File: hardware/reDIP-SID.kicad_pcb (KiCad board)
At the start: 6 copper layers, 17.8 x 35.6 mm, 92 parts, among them J1 Conn_01x04, J2 Conn_01x04, J3 Conn_01x10, J4 Conn_01x10, J5 TYPE-C-31-M-12, J6 Conn_02x05_Odd_Even, Q1 PDTA143ZMB, SW1 KXT331LHS, U1 NCP163AMX120TBG, U2 NCP167AMX330TBG, U3 SN74CBTD16211DGVR, U4 SGTL5000XNLA3, U5 NUF2042XV6, U6 APS6404L-3SQR-SN, U7 W25Q128JVPIM, U8 ICE40UP5K-SG48I, X1 ASCO-24.576MHZ-EK-T

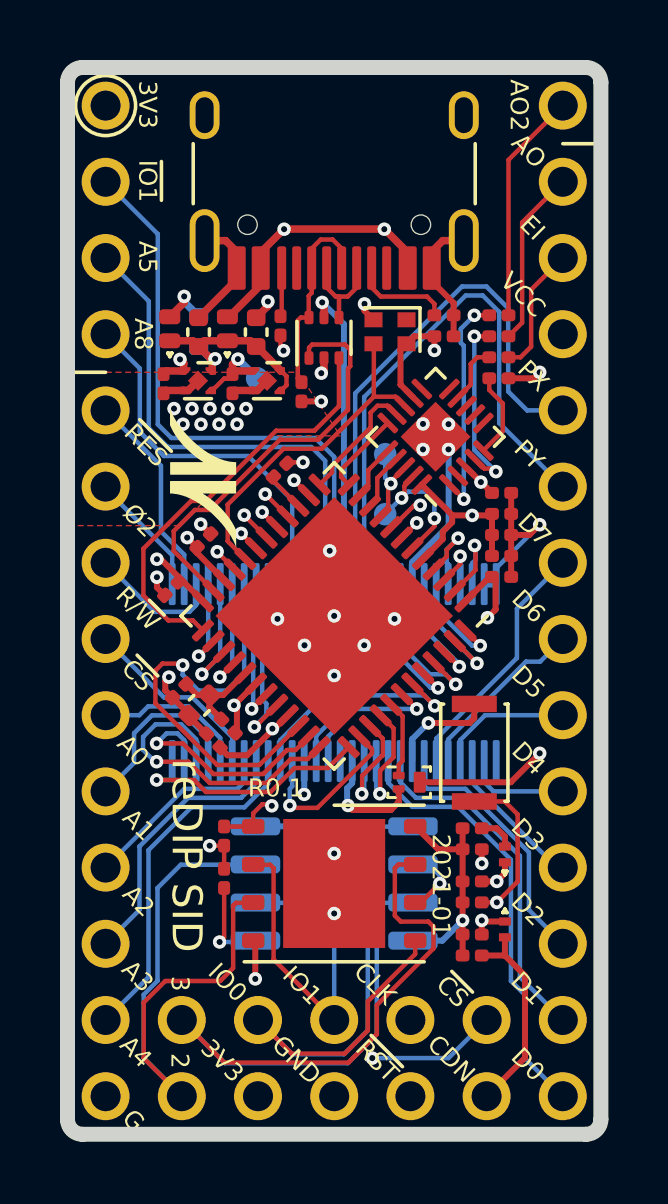
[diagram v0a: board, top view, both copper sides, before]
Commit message: Moved Vcc via away from pin-in-paste stencil aperture
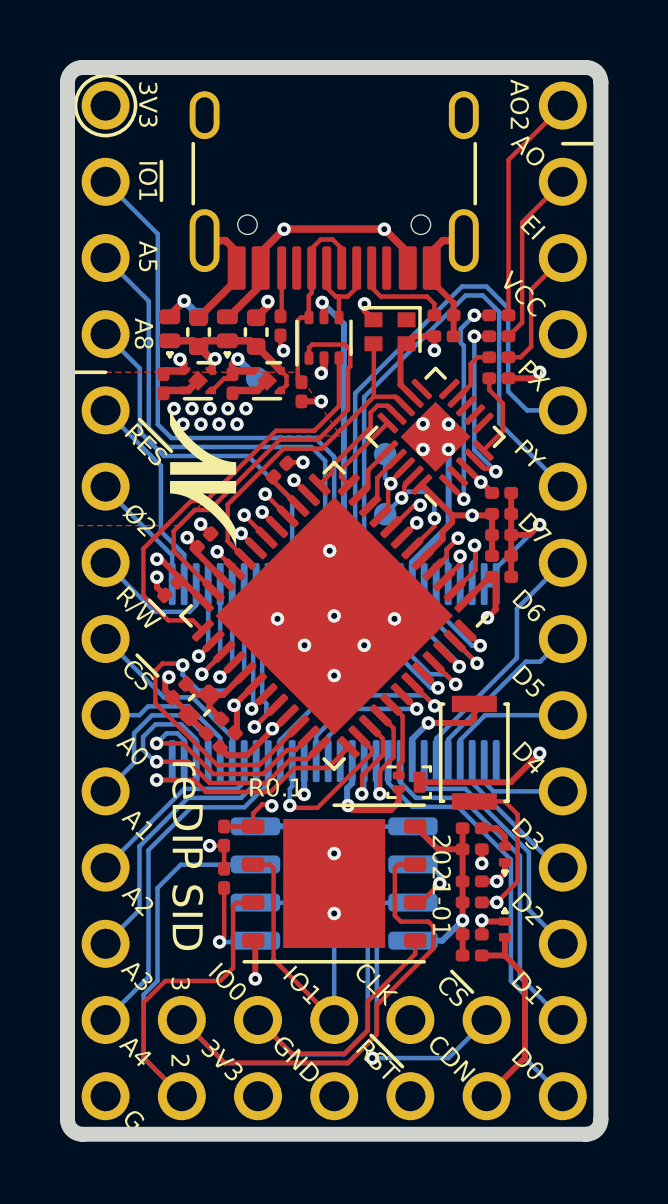
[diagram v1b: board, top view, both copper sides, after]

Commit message: Usability and manufacturability improvements
* Made all iCE40 RGB pins externally available
* Removed split in stencil apertures for pin-in-paste
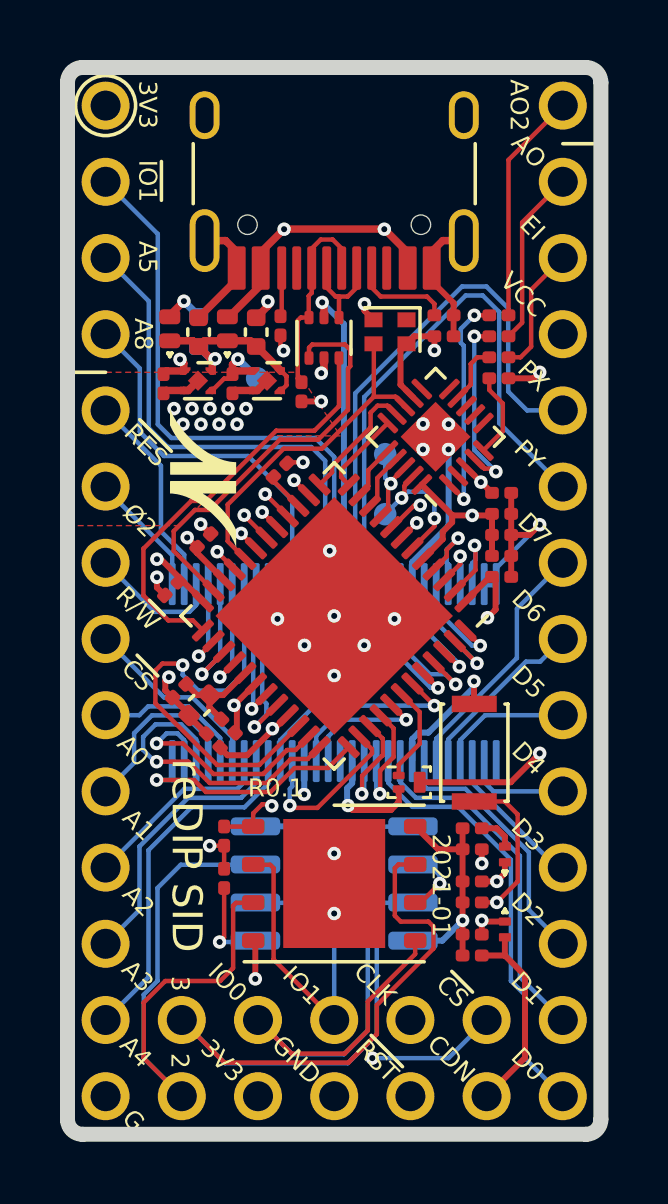
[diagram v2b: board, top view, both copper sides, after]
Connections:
- Q1 pad 1: /USB_CONN -> /USB_~CONN~
- U8 pad 41: /USB_CONN -> /ICE_~IO1~
- U8 pad 42: /ICE_~IO1~ -> /USB_~CONN~
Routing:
- net /USB_~CONN~: track 0.00 -> 3.31 mm
- net /USB_CONN: track 2.57 -> 0.00 mm
- net GND: track 48.4 -> 49.3 mm

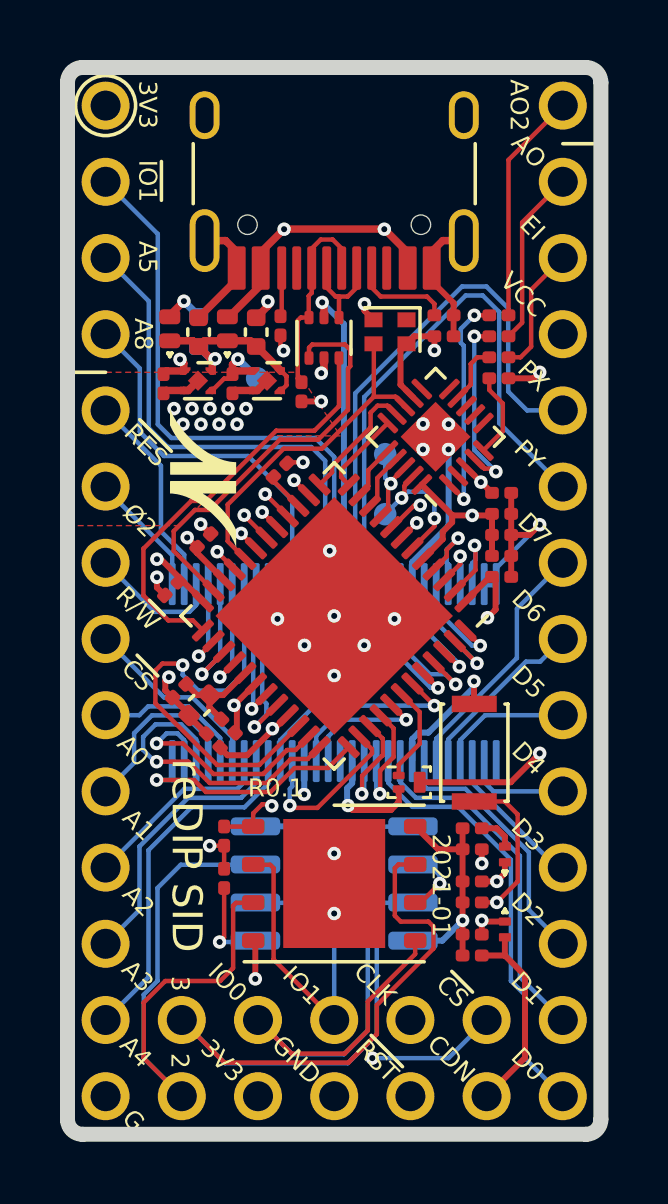
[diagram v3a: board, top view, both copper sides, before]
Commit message: Usability and manufacturability improvements
* Added extra vias for Vcc and 3.3V rails, for high power external devices
* Added extra thermal via for SGTL5000
* Assume 3x solder paste volume for paste-in-hole
* Adjustments to fab and silk screen layers
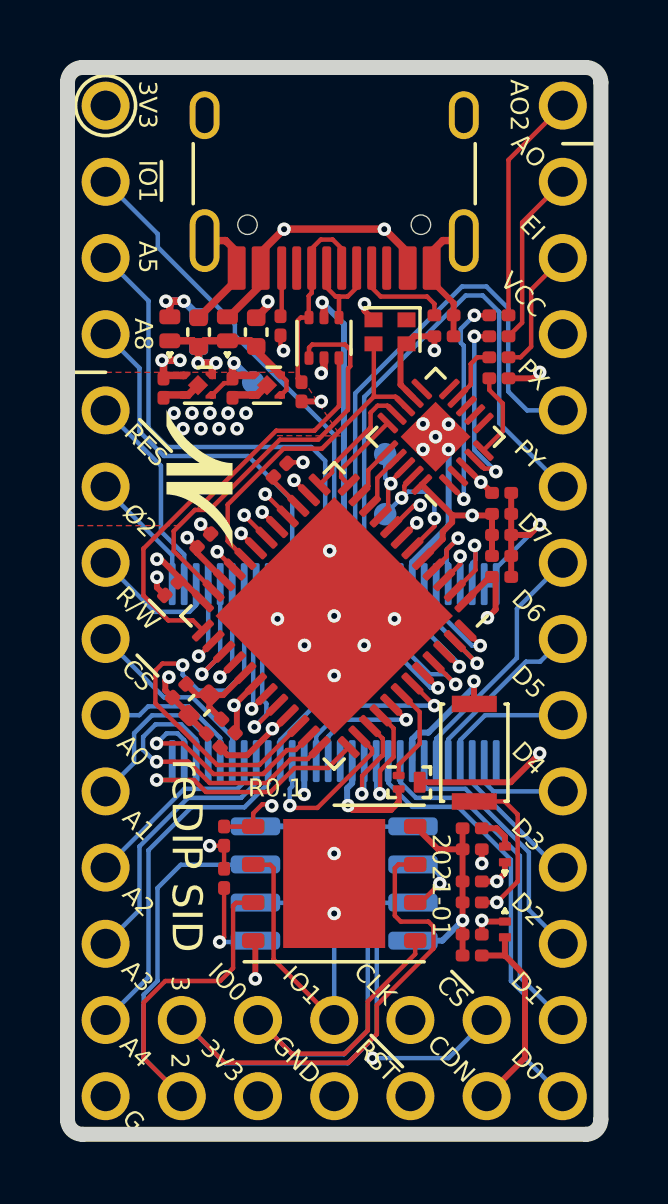
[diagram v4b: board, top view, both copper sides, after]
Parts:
- removed the SolderMask D0.5mm at (102.9, 110.1) (x2)
- removed the SolderMask D0.5mm at (102.3, 110.1) (x2)
- removed the SolderMask D0.5mm at (103.2, 110.6) (x2)
- removed the SolderMask D0.5mm at (102.6, 110.6) (x2)
- removed the SolderMask D0.5mm at (103.5, 110.1) (x2)
- removed the SolderMask D0.5mm at (103.8, 110.6) (x2)
- removed the SolderMask D0.5mm at (104.1, 110.1) (x2)
- removed the SolderMask D0.5mm at (104.4, 110.6) (x2)
- added SolderMask D0.5mm: SolderMask_D0.5mm, reDIP:SolderMask_D0.5mm, B.Cu at (111.0, 111.0)
- added SolderMask D0.5mm: SolderMask_D0.3mm, reDIP:SolderMask_D0.3mm, F.Cu at (103.5, 110.2)
- added SolderMask D0.5mm: SolderMask_D0.3mm, reDIP:SolderMask_D0.3mm, F.Cu at (102.9, 110.2)
- added SolderMask D0.5mm: SolderMask_D0.3mm, reDIP:SolderMask_D0.3mm, F.Cu at (102.3, 110.2)
- added SolderMask D0.5mm: SolderMask_D0.5mm, reDIP:SolderMask_D0.5mm, B.Cu at (103.2, 110.8)
- added SolderMask D0.5mm: SolderMask_D0.5mm, reDIP:SolderMask_D0.5mm, B.Cu at (102.6, 110.8)
- added SolderMask D0.5mm: SolderMask_D0.5mm, reDIP:SolderMask_D0.5mm, B.Cu at (102.3, 110.2)
- added SolderMask D0.5mm: SolderMask_D0.5mm, reDIP:SolderMask_D0.5mm, B.Cu at (102.9, 110.2)
- added SolderMask D0.5mm: SolderMask_D0.5mm, reDIP:SolderMask_D0.5mm, B.Cu at (103.5, 110.2)
- added SolderMask D0.5mm: SolderMask_D0.5mm, reDIP:SolderMask_D0.5mm, B.Cu at (103.8, 110.8)
- added SolderMask D0.5mm: SolderMask_D0.5mm, reDIP:SolderMask_D0.5mm, B.Cu at (104.1, 110.2)
- added SolderMask D0.5mm: SolderMask_D0.5mm, reDIP:SolderMask_D0.5mm, B.Cu at (104.4, 110.8)
- added SolderMask D0.5mm: SolderMask_D0.3mm, reDIP:SolderMask_D0.3mm, F.Cu at (104.4, 110.8)
- added SolderMask D0.5mm: SolderMask_D0.3mm, reDIP:SolderMask_D0.3mm, F.Cu at (103.8, 110.8)
- added SolderMask D0.5mm: SolderMask_D0.3mm, reDIP:SolderMask_D0.3mm, F.Cu at (103.2, 110.8)
- added SolderMask D0.5mm: SolderMask_D0.3mm, reDIP:SolderMask_D0.3mm, F.Cu at (102.6, 110.8)
- added SolderMask D0.5mm: SolderMask_D0.3mm, reDIP:SolderMask_D0.3mm, F.Cu at (104.1, 110.2)
- moved TP1 0.18 mm to (104.9, 109.2)
- moved C2 0.15 mm to (104.2, 109.4)
- moved C4 0.15 mm to (101.9, 109.4)
- moved SolderMask D0.5mm 0.15 mm to (104.7, 110.2) (x2)
- moved U1 0.15 mm to (105.4, 109.3)
- moved U2 0.15 mm to (103.1, 109.3)
- moved svg2mod 0.12 mm to (103.1, 112.4)
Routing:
- net /~IO1~: track 20.2 -> 17.4 mm
- net +5V: track 27.5 -> 29.1 mm, vias 2 -> 3
- net /Vcc: track 21.5 -> 23.0 mm, vias 1 -> 2
- net +3V3: track 25.1 -> 26.5 mm, vias 9 -> 10
- net GND: vias 35 -> 36

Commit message: Adjusted TVSOP-56 footprint to match datasheet
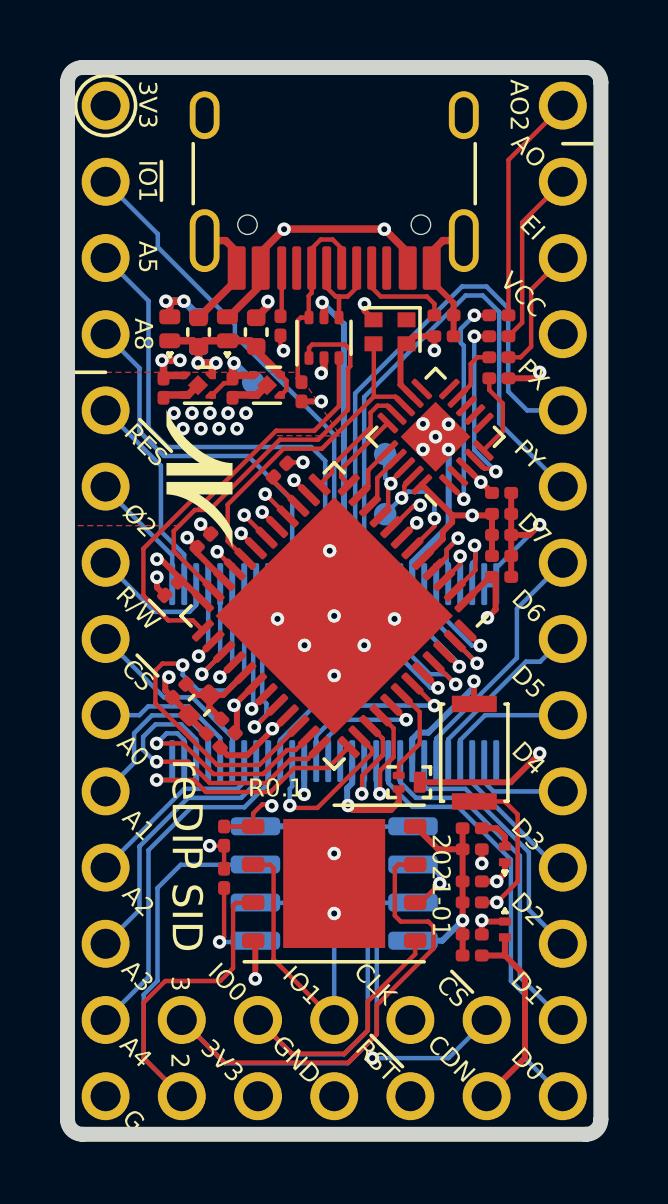
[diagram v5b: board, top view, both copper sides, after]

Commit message: Various fixes
* Added 10k pullup for SPI SCLK, following iCE40 Hardware Checklist
* Reworked USB routing to not rely on any particular ESD IC (note swapped pins)
* Widened a few tracks
* Added silk screen on back side for SPI header
* Increased courtyard for TVSOP-56 footprint
* Changed VCC to power symbol
* Corrected BOM for LDOs
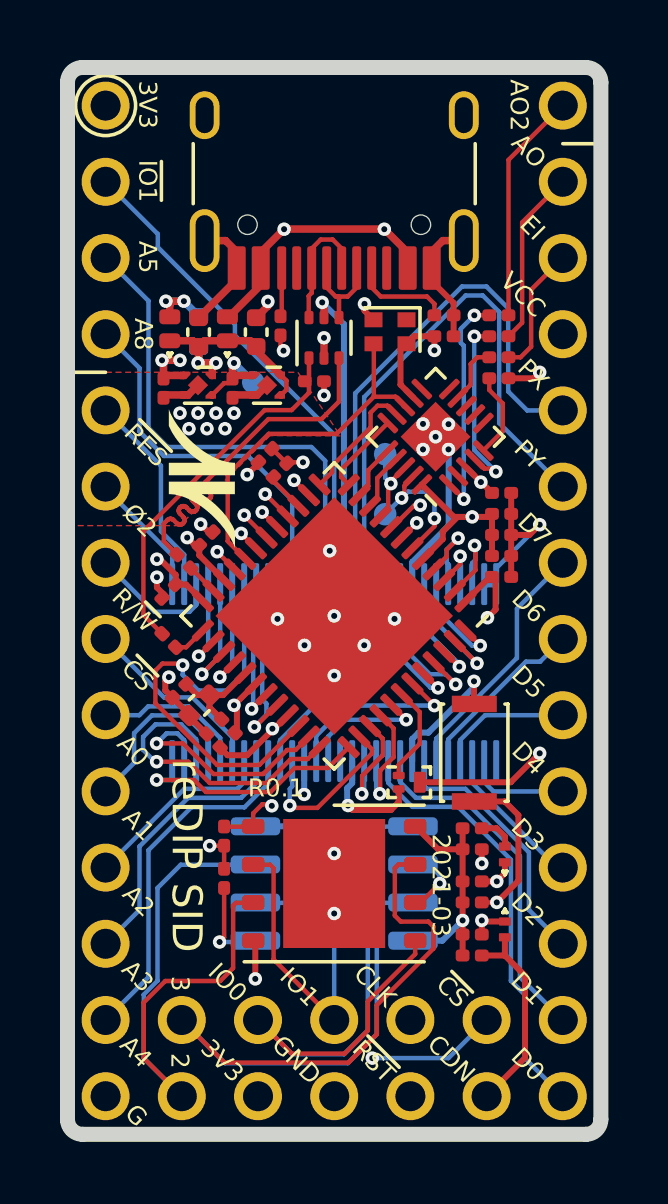
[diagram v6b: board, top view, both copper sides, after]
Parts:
- removed the SolderMask D0.5mm at (103.5, 110.2) (x2)
- removed the SolderMask D0.5mm at (102.9, 110.2) (x2)
- removed the SolderMask D0.5mm at (103.2, 110.8) (x2)
- removed the SolderMask D0.5mm at (102.6, 110.8) (x2)
- removed the SolderMask D0.5mm at (102.3, 110.2)
- removed the SolderMask D0.5mm at (103.8, 110.8) (x2)
- removed the SolderMask D0.5mm at (104.7, 110.2) (x2)
- removed the SolderMask D0.5mm at (104.4, 110.8) (x2)
- removed the SolderMask D0.5mm at (104.1, 110.2)
- added R12: 0, Resistor_SMD:R_0201_0603Metric, F.Cu at (102.1, 117.8)
- added R13: 0, Resistor_SMD:R_0201_0603Metric, F.Cu at (102.6, 115.2)
- added R7: 10k, Resistor_SMD:R_0201_0603Metric, F.Cu at (105.3, 111.7)
- added SolderMask D0.5mm: SolderMask_D0.5mm, reDIP:SolderMask_D0.5mm, B.Cu at (103.4, 110.8)
- added SolderMask D0.5mm: SolderMask_D0.5mm, reDIP:SolderMask_D0.5mm, B.Cu at (102.8, 110.8)
- added SolderMask D0.5mm: SolderMask_D0.5mm, reDIP:SolderMask_D0.5mm, B.Cu at (102.5, 110.2)
- added SolderMask D0.5mm: SolderMask_D0.5mm, reDIP:SolderMask_D0.5mm, B.Cu at (103.1, 110.2)
- added SolderMask D0.5mm: SolderMask_D0.5mm, reDIP:SolderMask_D0.5mm, B.Cu at (103.7, 110.2)
- added SolderMask D0.5mm: SolderMask_D0.5mm, reDIP:SolderMask_D0.5mm, B.Cu at (104.0, 110.8)
- added SolderMask D0.5mm: SolderMask_D0.3mm, reDIP:SolderMask_D0.3mm, F.Cu at (104.0, 110.8)
- added SolderMask D0.5mm: SolderMask_D0.3mm, reDIP:SolderMask_D0.3mm, F.Cu at (103.4, 110.8)
- added SolderMask D0.5mm: SolderMask_D0.3mm, reDIP:SolderMask_D0.3mm, F.Cu at (102.8, 110.8)
- added SolderMask D0.5mm: SolderMask_D0.3mm, reDIP:SolderMask_D0.3mm, F.Cu at (104.3, 110.2)
- added SolderMask D0.5mm: SolderMask_D0.3mm, reDIP:SolderMask_D0.3mm, F.Cu at (103.7, 110.2)
- added SolderMask D0.5mm: SolderMask_D0.3mm, reDIP:SolderMask_D0.3mm, F.Cu at (103.1, 110.2)
- moved R3 0.55 mm to (107.0, 109.2), turned to 0 degrees
- moved SolderMask D0.5mm 0.20 mm to (104.3, 110.2)
- moved SolderMask D0.5mm 0.20 mm to (102.5, 110.2)
- moved C18 0.13 mm to (102.1, 116.2)
- moved C14 0.10 mm to (103.3, 114.4)
- moved svg2mod 0.08 mm to (103.2, 112.4)
- renumbered R9 to R10, R10 to R11, R11 to R14, R7 to R8, R8 to R9
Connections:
- net /Vcc renamed VCC
- R3 pad 1: /D+ -> /USB_D+
- U8 pad 23: /USB_D+ -> Net-(R13-Pad1)
- U8 pad 25: /USB_D- -> Net-(R12-Pad1)
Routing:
- net /D+: track 6.77 -> 4.24 mm
- net /USB_D-: track 14.1 -> 12.2 mm
- net /USB_D+: track 13.9 -> 12.4 mm
- net Net-(R13-Pad1): track 0.00 -> 1.22 mm
- net Net-(R12-Pad1): track 0.00 -> 1.14 mm
- net +3V3: track 26.5 -> 27.2 mm, vias 10 -> 11
- net /SPI_SCLK: track 28.0 -> 28.7 mm
- net /SYS_CLK: track 11.3 -> 11.9 mm
- net GND: track 49.3 -> 49.5 mm, vias 36 -> 34
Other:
- board text added: "2021-03"
- board text added: "IO2"
- board text added: "IO3"
- board text removed: "2021-01"

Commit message: Replaced non-stocked parts
* Replaced 1.2V LDO with more readily available part
* Changed oscillator reeling order number
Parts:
- U1, U2: footprint ONSemi:CASE711AJ_1.0x1.0mm_P0.65mm -> ONSemi:CASE_711AJ_1.0x1.0mm_P0.65mm
- U5: footprint ONSemi:CASE463A_1.6x1.2mm_P0.5mm -> ONSemi:CASE_463A_1.6x1.2mm_P0.5mm
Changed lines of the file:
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@@
     (pad "" smd circle (at 0 0) (size 0.5 0.5) (layers B.Mask))
   )
-  (module ONSemi:CASE711AJ_1.0x1.0mm_P0.65mm (layer F.Cu)
+  (module ONSemi:CASE_711AJ_1.0x1.0mm_P0.65mm (layer F.Cu)
     (at 105.38 109.32)
     (descr XDFN4)
@@
     )
   )
-  (module ONSemi:CASE711AJ_1.0x1.0mm_P0.65mm (layer F.Cu)
+  (module ONSemi:CASE_711AJ_1.0x1.0mm_P0.65mm (layer F.Cu)
     (at 103.08 109.32)
     (descr XDFN4)
@@
     )
   )
-  (module ONSemi:CASE463A_1.6x1.2mm_P0.5mm (layer F.Cu)
+  (module ONSemi:CASE_463A_1.6x1.2mm_P0.5mm (layer F.Cu)
     (at 107.28 107.74 90)
     (descr SOT563)
